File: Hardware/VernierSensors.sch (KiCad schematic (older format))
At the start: 8 parts

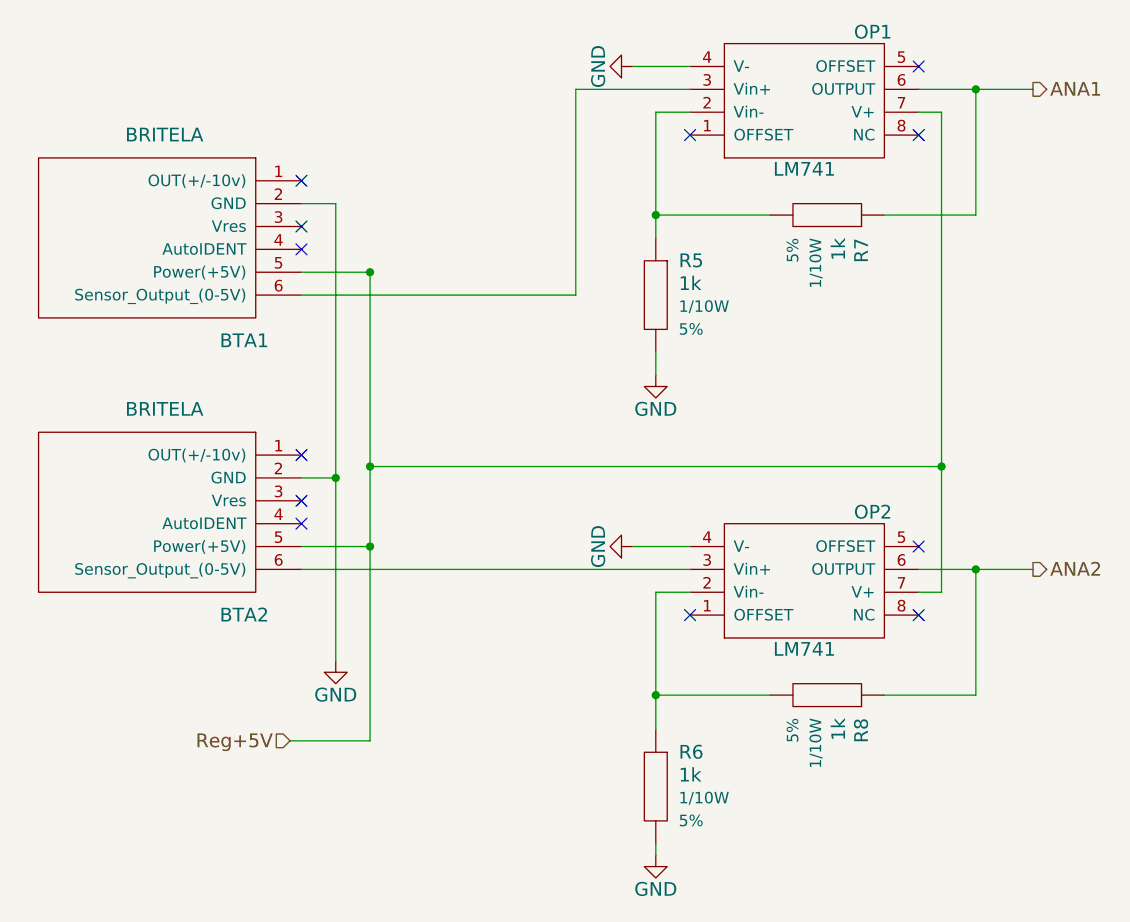
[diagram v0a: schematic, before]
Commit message: Fix annotation problem, Add IC datasheets
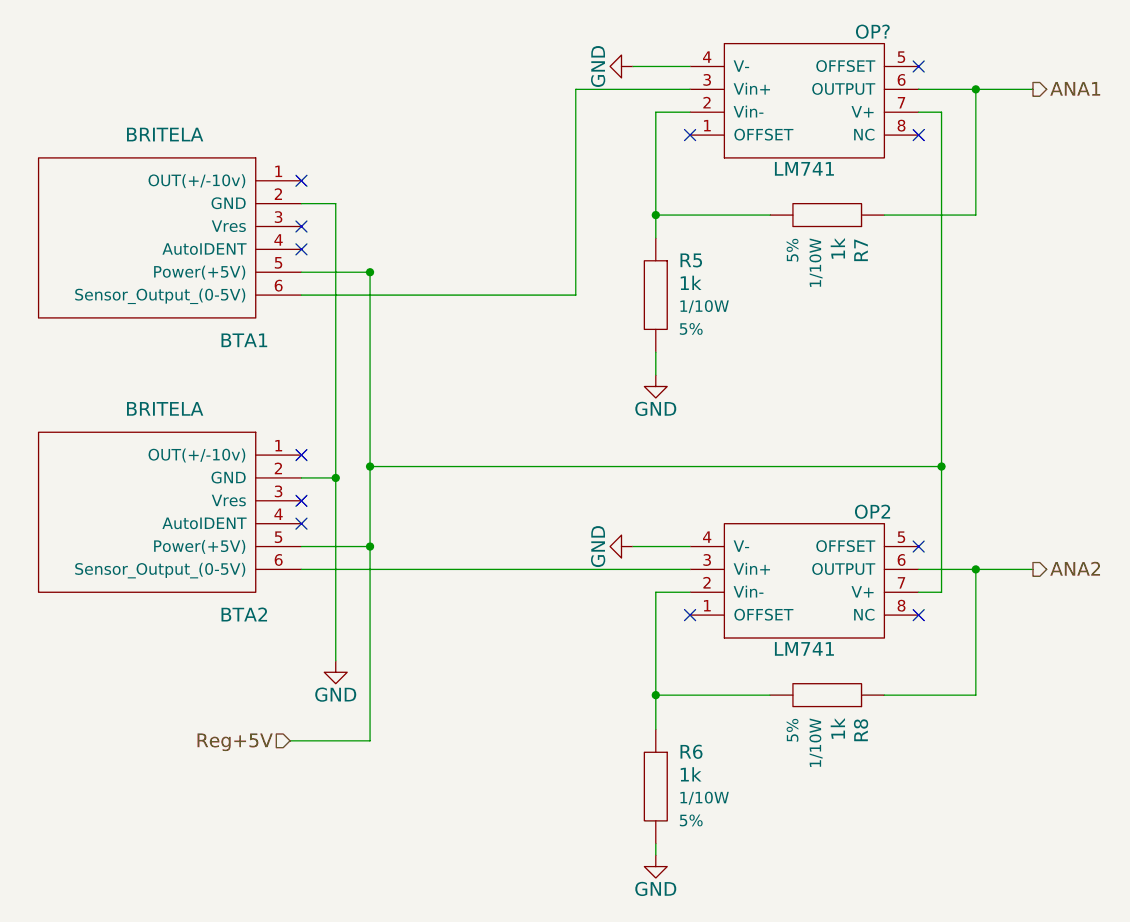
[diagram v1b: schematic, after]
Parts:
- removed OP1: LM741, symbol LM741
- added OP?: LM741, symbol LM741
- OP2: Vendor (none) -> Digi-Key; Vendor SKU (none) -> 296-15051-1-ND
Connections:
- net ANA1: now also OP?.6 (OUTPUT)
- net GND: now also OP?.4 (V-)
- net Reg+5V: now also OP?.7 (V+)
- net at BTA1.6 (Sensor_Output_(0-5V)): now also OP?.3 (Vin+)
- net at R5.1, R7.2: now also OP?.2 (Vin-)
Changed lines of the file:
@@
 LIBS:STMicroelectronics
 LIBS:Connectors
+LIBS:74xx
+LIBS:atmel
+LIBS:audio
+LIBS:transistors
 LIBS:Main Board-cache
 EELAYER 25 0
@@
 Connection ~ 2900 3300
 $Comp
-L GND #PWR16
+L GND #PWR016
 U 1 1 551E15A1
 P 2900 4100
-F 0 "#PWR16" H 2900 3850 60  0001 C CNN
+F 0 "#PWR016" H 2900 3850 60  0001 C CNN
 F 1 "GND" H 2900 3950 60  0000 C CNN
 F 2 "" H 2900 4100 60  0000 C CNN
@@
 Wire Wire Line
 	2750 3700 4450 3700
-$Comp
-L LM741 OP1
-U 1 1 5536B2A8
-P 4950 1650
-F 0 "OP1" H 5250 1350 60  0000 C CNN
-F 1 "LM741" H 4950 1950 60  0000 C CNN
-F 2 "" H 4850 1600 60  0000 C CNN
-F 3 "" H 4850 1600 60  0000 C CNN
-	1    4950 1650
-	1    0    0    1
-$EndComp
 Wire Wire Line
 	3950 2500 3950 1600
@@
 	5700 1600 5950 1600
 $Comp
-L GND #PWR19
+L GND #PWR017
 U 1 1 5536C048
 P 4300 2850
-F 0 "#PWR19" H 4300 2600 60  0001 C CNN
+F 0 "#PWR017" H 4300 2600 60  0001 C CNN
 F 1 "GND" H 4300 2700 60  0000 C CNN
 F 2 "" H 4300 2850 60  0000 C CNN
@@
 F 2 "" H 4850 3700 60  0000 C CNN
 F 3 "" H 4850 3700 60  0000 C CNN
+F 4 "Digi-Key" H 4950 3750 60  0001 C CNN "Vendor"
+F 5 "296-15051-1-ND" H 4950 3750 60  0001 C CNN "Vendor SKU"
 	1    4950 3750
 	1    0    0    1
@@
 	5700 3700 5950 3700
 $Comp
-L GND #PWR20
+L GND #PWR018
 U 1 1 5536C381
 P 4300 4950
-F 0 "#PWR20" H 4300 4700 60  0001 C CNN
+F 0 "#PWR018" H 4300 4700 60  0001 C CNN
 F 1 "GND" H 4300 4800 60  0000 C CNN
 F 2 "" H 4300 4950 60  0000 C CNN
@@
 Connection ~ 5700 3700
 $Comp
-L GND #PWR18
+L GND #PWR019
 U 1 1 5536CDD6
 P 4200 3600
-F 0 "#PWR18" H 4200 3350 60  0001 C CNN
+F 0 "#PWR019" H 4200 3350 60  0001 C CNN
 F 1 "GND" H 4200 3450 60  0000 C CNN
 F 2 "" H 4200 3600 60  0000 C CNN
@@
 	4450 1500 4200 1500
 $Comp
-L GND #PWR17
+L GND #PWR020
 U 1 1 5536CE79
 P 4200 1500
-F 0 "#PWR17" H 4200 1250 60  0001 C CNN
+F 0 "#PWR020" H 4200 1250 60  0001 C CNN
 F 1 "GND" H 4200 1350 60  0000 C CNN
 F 2 "" H 4200 1500 60  0000 C CNN
@@
 $EndComp
 Wire Wire Line
-	5450 3800 5550 3800
-Wire Wire Line
-	5550 3800 5550 3250
-Wire Wire Line
-	5550 3250 5550 1700
+	5550 3800 5450 3800
+Wire Wire Line
+	5550 1700 5550 3250
+Wire Wire Line
+	5550 3250 5550 3800
 Wire Wire Line
 	5550 1700 5450 1700
@@
 NoConn ~ 2750 3400
 NoConn ~ 2750 3500
+$Comp
+L LM741 OP?
+U 1 1 5535FF61
+P 4950 1650
+F 0 "OP?" H 5250 1350 60  0000 C CNN
+F 1 "LM741" H 4950 1950 60  0000 C CNN
+F 2 "" H 4850 1600 60  0000 C CNN
+F 3 "" H 4850 1600 60  0000 C CNN
+F 4 "Digi-Key" H 4950 1650 60  0001 C CNN "Vendor"
+F 5 "296-15051-1-ND" H 4950 1650 60  0001 C CNN "Vendor SKU"
+	1    4950 1650
+	1    0    0    1
+$EndComp
 $EndSCHEMATC
